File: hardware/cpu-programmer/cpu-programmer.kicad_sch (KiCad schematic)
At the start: 13 parts, among them J1 Conn_01x15_Socket, J2 Conn_01x04_Socket, SW1 SW_Push, SW2 SW_Push

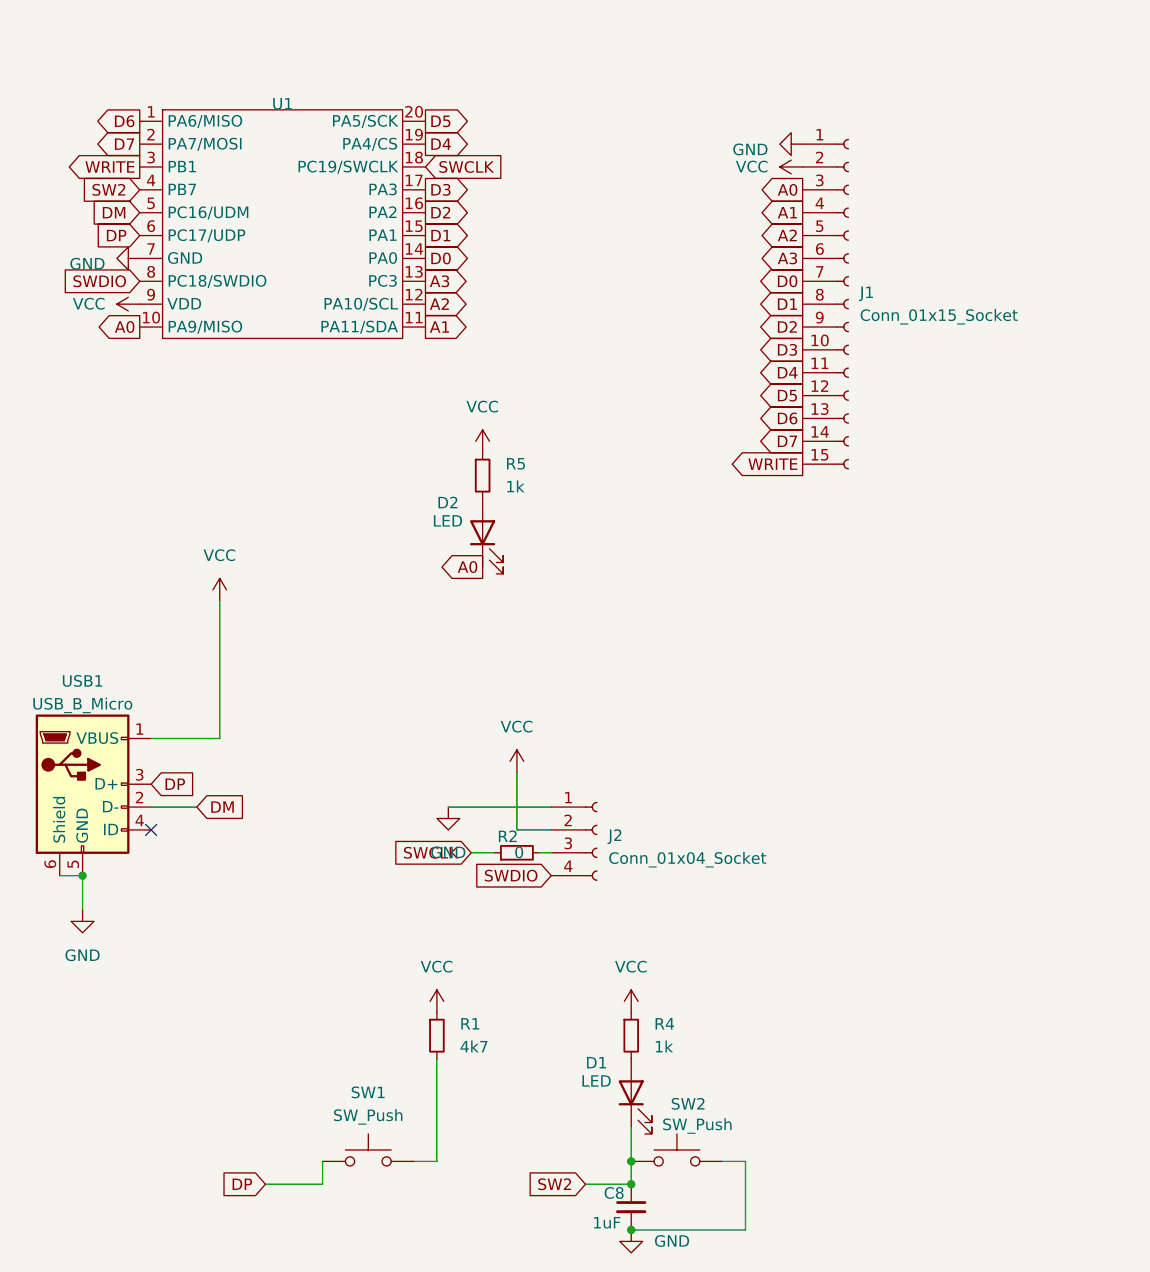
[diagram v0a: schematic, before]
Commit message: Clean up schematic
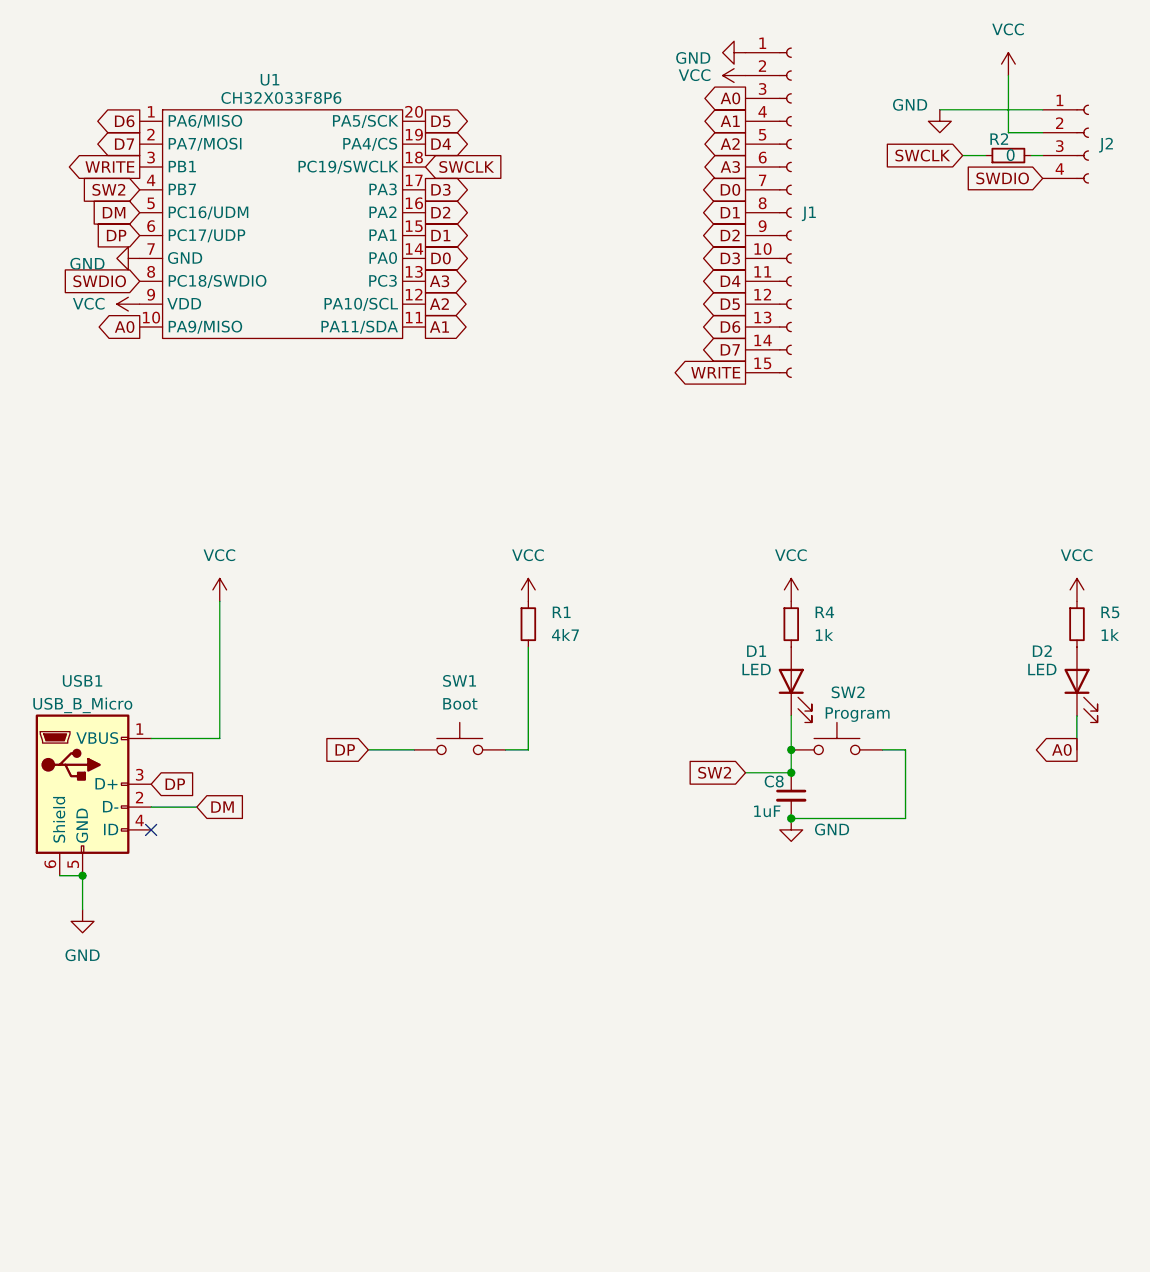
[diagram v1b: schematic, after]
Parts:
- SW1: value SW_Push -> Boot
- SW2: value SW_Push -> Program
- U1: value ~ -> CH32X033F8P6
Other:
- moved on the sheet: C8, D1, D2, J1, J2, R1, R2, R4, R5, SW1, SW2

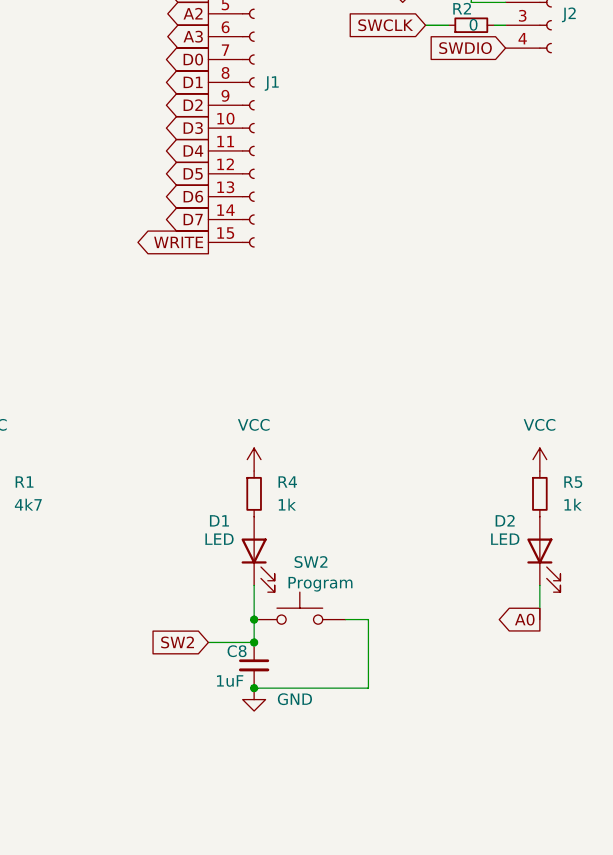
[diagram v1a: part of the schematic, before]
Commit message: Updated PCB, parts use at least package 0603
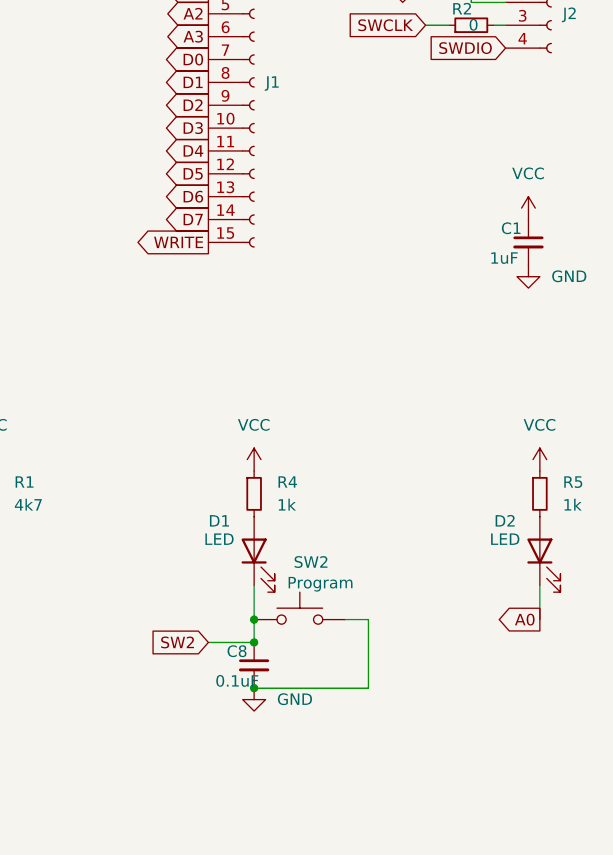
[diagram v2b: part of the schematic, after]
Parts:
- added C1: 1uF, Capacitor_SMD:C_0603_1608Metric, symbol Device:C_Small
- C8: value 1uF -> 0.1uF; footprint Capacitor_SMD:C_0402_1005Metric -> Capacitor_SMD:C_0603_1608Metric
- D1, D2: footprint LED_SMD:LED_0402_1005Metric -> LED_SMD:LED_0603_1608Metric
- R4, R5: footprint Resistor_SMD:R_0402_1005Metric -> Resistor_SMD:R_0603_1608Metric
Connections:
- net GND: now also C1.2
- net VCC: now also C1.1
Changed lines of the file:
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@@
+	(symbol
+		(lib_id "Device:C_Small")
+		(at 137.16 59.69 0)
+		(unit 1)
+		(exclude_from_sim no)
+		(in_bom yes)
+		(on_board yes)
+		(dnp no)
+		(property "Reference" "C1"
+			(at 134.112 58.166 0)
+			(effects
+				(font
+					(size 1.27 1.27)
+				)
+				(justify left)
+			)
+		)
+		(property "Value" "1uF"
+			(at 132.842 61.468 0)
+			(effects
+				(font
+					(size 1.27 1.27)
+				)
+				(justify left)
+			)
+		)
+		(property "Footprint" "Capacitor_SMD:C_0603_1608Metric"
+			(at 137.16 59.69 0)
+			(effects
+				(font
+					(size 1.27 1.27)
+				)
+				(hide yes)
+			)
+		)
+		(property "Datasheet" "~"
+			(at 137.16 59.69 0)
+			(effects
+				(font
+					(size 1.27 1.27)
+				)
+				(hide yes)
+			)
+		)
+		(property "Description" "Unpolarized capacitor, small symbol"
+			(at 137.16 59.69 0)
+			(effects
+				(font
+					(size 1.27 1.27)
+				)
+				(hide yes)
+			)
+		)
+		(pin "1"
+		)
+		(pin "2"
+		)
+		(instances
+			(project "cpu-programmer"
+				(path "/6e692abf-3379-42ed-b901-258ac932806b"
+					(reference "C1")
+					(unit 1)
+				)
+			)
+		)
+	)
+	(symbol
+		(lib_id "power:+3.3V")
+		(at 137.16 57.15 0)
+		(unit 1)
+		(exclude_from_sim no)
+		(in_bom yes)
+		(on_board yes)
+		(dnp no)
+		(fields_autoplaced yes)
+		(property "Reference" "#PWR09"
+			(at 137.16 60.96 0)
+			(effects
+				(font
+					(size 1.27 1.27)
+				)
+				(hide yes)
+			)
+		)
+		(property "Value" "VCC"
+			(at 137.16 52.07 0)
+			(effects
+				(font
+					(size 1.27 1.27)
+				)
+			)
+		)
+		(property "Footprint" ""
+			(at 137.16 57.15 0)
+			(effects
+				(font
+					(size 1.27 1.27)
+				)
+				(hide yes)
+			)
+		)
+		(property "Datasheet" ""
+			(at 137.16 57.15 0)
+			(effects
+				(font
+					(size 1.27 1.27)
+				)
+				(hide yes)
+			)
+		)
+		(property "Description" ""
+			(at 137.16 57.15 0)
+			(effects
+				(font
+					(size 1.27 1.27)
+				)
+			)
+		)
+		(pin "1"
+		)
+		(instances
+			(project "cpu-programmer"
+				(path "/6e692abf-3379-42ed-b901-258ac932806b"
+					(reference "#PWR09")
+					(unit 1)
+				)
+			)
+		)
+	)
+	(symbol
+		(lib_id "power:GND")
+		(at 137.16 62.23 0)
+		(unit 1)
+		(exclude_from_sim no)
+		(in_bom yes)
+		(on_board yes)
+		(dnp no)
+		(fields_autoplaced yes)
+		(property "Reference" "#PWR010"
+			(at 137.16 68.58 0)
+			(effects
+				(font
+					(size 1.27 1.27)
+				)
+				(hide yes)
+			)
+		)
+		(property "Value" "GND"
+			(at 139.7 63.4999 0)
+			(effects
+				(font
+					(size 1.27 1.27)
+				)
+				(justify left)
+			)
+		)
+		(property "Footprint" ""
+			(at 137.16 62.23 0)
+			(effects
+				(font
+					(size 1.27 1.27)
+				)
+				(hide yes)
+			)
+		)
+		(property "Datasheet" ""
+			(at 137.16 62.23 0)
+			(effects
+				(font
+					(size 1.27 1.27)
+				)
+				(hide yes)
+			)
+		)
+		(property "Description" "Power symbol creates a global label with name \"GND\" , ground"
+			(at 137.16 62.23 0)
+			(effects
+				(font
+					(size 1.27 1.27)
+				)
+				(hide yes)
+			)
+		)
+		(pin "1"
+		)
+		(instances
+			(project "cpu-programmer"
+				(path "/6e692abf-3379-42ed-b901-258ac932806b"
+					(reference "#PWR010")
+					(unit 1)
+				)
+			)
+		)
+	)
 	(symbol
 		(lib_id "Device:C_Small")
@@
 			)
 		)
-		(property "Value" "1uF"
+		(property "Value" "0.1uF"
 			(at 102.362 108.458 0)
 			(effects
@@
 			)
 		)
-		(property "Footprint" "Capacitor_SMD:C_0402_1005Metric"
+		(property "Footprint" "Capacitor_SMD:C_0603_1608Metric"
 			(at 106.68 106.68 0)
 			(effects
@@
 			)
 		)
-		(property "Footprint" "LED_SMD:LED_0402_1005Metric"
+		(property "Footprint" "LED_SMD:LED_0603_1608Metric"
 			(at 106.68 93.98 0)
 			(effects
@@
 			)
 		)
-		(property "Footprint" "Resistor_SMD:R_0402_1005Metric"
+		(property "Footprint" "Resistor_SMD:R_0603_1608Metric"
 			(at 138.43 87.63 0)
 			(effects
@@
 			)
 		)
-		(property "Footprint" "Resistor_SMD:R_0402_1005Metric"
+		(property "Footprint" "Resistor_SMD:R_0603_1608Metric"
 			(at 106.68 87.63 0)
 			(effects
@@
 			)
 		)
-		(property "Footprint" "LED_SMD:LED_0402_1005Metric"
+		(property "Footprint" "LED_SMD:LED_0603_1608Metric"
 			(at 138.43 93.98 0)
 			(effects

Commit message: Added gerber
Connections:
- net SWCLK: now also J2.3 (Pin_3), R2.2
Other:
- moved on the sheet: R2
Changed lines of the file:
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@@
+	)
+	(junction
+		(at 129.54 35.56)
+		(diameter 0)
+		(color 0 0 0 0)
 	)
 	(junction
@@
 	)
 	(junction
+		(at 121.92 35.56)
+		(diameter 0)
+		(color 0 0 0 0)
+	)
+	(junction
 		(at 106.68 104.14)
 		(diameter 0)
@@
 	(wire
 		(pts
-			(xy 138.43 101.6) (xy 138.43 97.79)
+			(xy 129.54 34.29) (xy 129.54 35.56)
 		)
 		(stroke
@@
 	(wire
 		(pts
-			(xy 25.4 115.57) (xy 27.94 115.57)
+			(xy 121.92 35.56) (xy 121.92 34.29)
 		)
 		(stroke
@@
 	(wire
 		(pts
-			(xy 77.47 90.17) (xy 77.47 101.6)
+			(xy 138.43 101.6) (xy 138.43 97.79)
 		)
 		(stroke
@@
 	(wire
 		(pts
-			(xy 27.94 115.57) (xy 27.94 119.38)
+			(xy 25.4 115.57) (xy 27.94 115.57)
 		)
 		(stroke
@@
 	(wire
 		(pts
-			(xy 125.73 35.56) (xy 128.27 35.56)
+			(xy 77.47 90.17) (xy 77.47 101.6)
 		)
 		(stroke
@@
 	(wire
 		(pts
-			(xy 134.62 33.02) (xy 130.81 33.02)
+			(xy 27.94 115.57) (xy 27.94 119.38)
 		)
 		(stroke
@@
 	(wire
 		(pts
-			(xy 130.81 33.02) (xy 130.81 26.67)
+			(xy 129.54 35.56) (xy 134.62 35.56)
 		)
 		(stroke
@@
 	(wire
 		(pts
-			(xy 74.93 101.6) (xy 77.47 101.6)
+			(xy 120.65 35.56) (xy 121.92 35.56)
 		)
 		(stroke
@@
 	(wire
 		(pts
-			(xy 133.35 35.56) (xy 134.62 35.56)
+			(xy 134.62 33.02) (xy 130.81 33.02)
 		)
 		(stroke
@@
 	(wire
 		(pts
-			(xy 106.68 109.22) (xy 119.38 109.22)
+			(xy 130.81 33.02) (xy 130.81 26.67)
 		)
 		(stroke
@@
 	(wire
 		(pts
-			(xy 35.56 100.33) (xy 43.18 100.33)
+			(xy 74.93 101.6) (xy 77.47 101.6)
 		)
 		(stroke
@@
 	(wire
 		(pts
-			(xy 119.38 101.6) (xy 119.38 109.22)
+			(xy 128.27 35.56) (xy 129.54 35.56)
 		)
 		(stroke
@@
 	(wire
 		(pts
-			(xy 123.19 30.48) (xy 134.62 30.48)
+			(xy 106.68 109.22) (xy 119.38 109.22)
 		)
 		(stroke
@@
 	(wire
 		(pts
-			(xy 106.68 101.6) (xy 106.68 104.14)
+			(xy 35.56 100.33) (xy 43.18 100.33)
 		)
 		(stroke
@@
 	(wire
 		(pts
-			(xy 106.68 101.6) (xy 106.68 97.79)
+			(xy 119.38 101.6) (xy 119.38 109.22)
 		)
 		(stroke
@@
 	(wire
 		(pts
-			(xy 59.69 101.6) (xy 64.77 101.6)
+			(xy 115.57 30.48) (xy 134.62 30.48)
 		)
 		(stroke
@@
 	(wire
 		(pts
-			(xy 43.18 85.09) (xy 43.18 100.33)
+			(xy 121.92 35.56) (xy 123.19 35.56)
 		)
 		(stroke
@@
 	(wire
 		(pts
-			(xy 116.84 101.6) (xy 119.38 101.6)
+			(xy 106.68 101.6) (xy 106.68 104.14)
 		)
 		(stroke
@@
 		)
 	)
+	(wire
+		(pts
+			(xy 106.68 101.6) (xy 106.68 97.79)
+		)
+		(stroke
+			(width 0)
+			(type default)
+		)
+	)
+	(wire
+		(pts
+			(xy 121.92 34.29) (xy 129.54 34.29)
+		)
+		(stroke
+			(width 0)
+			(type default)
+		)
+	)
+	(wire
+		(pts
+			(xy 59.69 101.6) (xy 64.77 101.6)
+		)
+		(stroke
+			(width 0)
+			(type default)
+		)
+	)
+	(wire
+		(pts
+			(xy 43.18 85.09) (xy 43.18 100.33)
+		)
+		(stroke
+			(width 0)
+			(type default)
+		)
+	)
+	(wire
+		(pts
+			(xy 116.84 101.6) (xy 119.38 101.6)
+		)
+		(stroke
+			(width 0)
+			(type default)
+		)
+	)
 	(global_label "D0"
 		(shape output)
@@
 	(global_label "SWCLK"
 		(shape input)
-		(at 125.73 35.56 180)
+		(at 120.65 35.56 180)
 		(fields_autoplaced yes)
 		(effects
@@
 		)
 		(property "Intersheetrefs" "${INTERSHEET_REFS}"
-			(at 116.5952 35.56 0)
+			(at 111.5152 35.56 0)
 			(effects
 				(font
@@
 	(symbol
 		(lib_id "power:GND")
-		(at 123.19 30.48 0)
+		(at 115.57 30.48 0)
 		(unit 1)
 		(exclude_from_sim no)
@@
 		(dnp no)
 		(property "Reference" "#PWR017"
-			(at 123.19 36.83 0)
+			(at 115.57 36.83 0)
 			(effects
 				(font
@@
 		)
 		(property "Value" "GND"
-			(at 119.888 29.972 0)
+			(at 112.268 29.972 0)
 			(effects
 				(font
@@
 		)
 		(property "Footprint" ""
-			(at 123.19 30.48 0)
+			(at 115.57 30.48 0)
 			(effects
 				(font
@@
 		)
 		(property "Datasheet" ""
-			(at 123.19 30.48 0)
+			(at 115.57 30.48 0)
 			(effects
 				(font
@@
 		)
 		(property "Description" ""
-			(at 123.19 30.48 0)
+			(at 115.57 30.48 0)
 			(effects
 				(font
@@
 	(symbol
 		(lib_id "Device:R_Small")
-		(at 130.81 35.56 90)
+		(at 125.73 35.56 90)
 		(unit 1)
 		(exclude_from_sim no)
@@
 		(dnp no)
 		(property "Reference" "R2"
-			(at 129.794 33.782 90)
+			(at 124.714 33.782 90)
 			(effects
 				(font
@@
 		)
 		(property "Value" "0"
-			(at 131.064 35.56 90)
+			(at 125.984 35.56 90)
 			(effects
 				(font
@@
 		)
 		(property "Footprint" "Resistor_SMD:R_1206_3216Metric"
-			(at 130.81 35.56 0)
+			(at 125.73 35.56 0)
 			(effects
 				(font
@@
 		)
 		(property "Datasheet" "~"
-			(at 130.81 35.56 0)
+			(at 125.73 35.56 0)
 			(effects
 				(font
@@
 		)
 		(property "Description" "Resistor, small symbol"
-			(at 130.81 35.56 0)
-			(effects
-				(font
+			(at 125.73 35.56 0)
+			(effects
+				(font

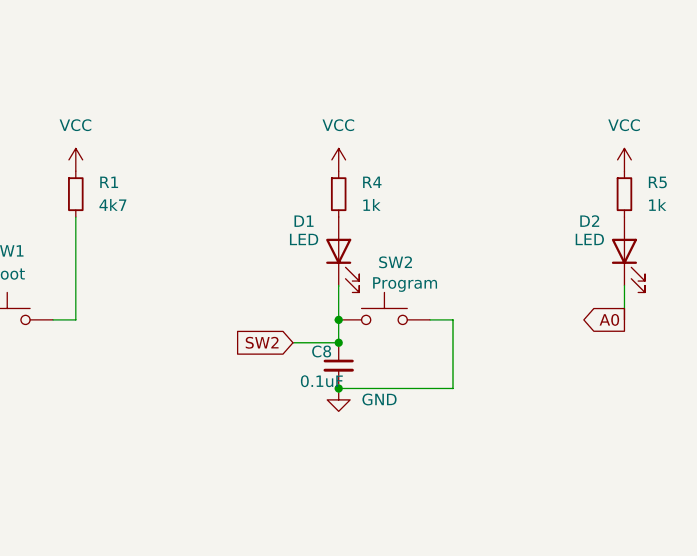
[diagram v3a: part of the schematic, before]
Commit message: Updated PCB
Fixed silkscreen lables
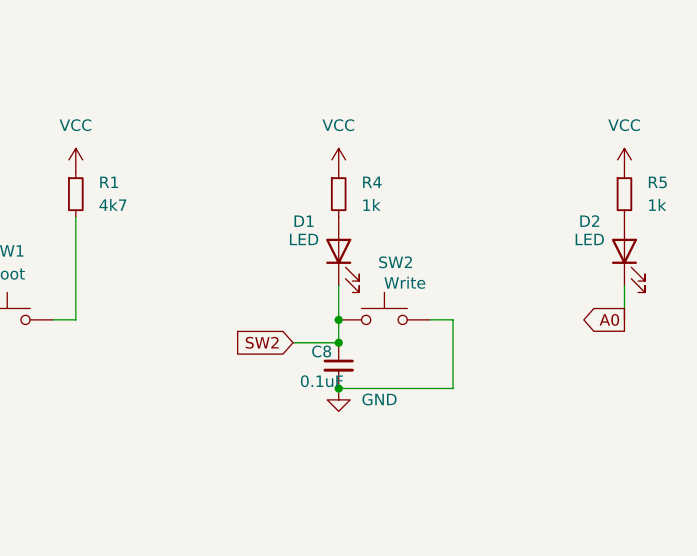
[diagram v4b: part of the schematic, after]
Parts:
- SW2: value Program -> Write
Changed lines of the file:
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@@
 			)
 		)
-		(property "Value" "Program"
+		(property "Value" "Write"
 			(at 114.046 97.536 0)
 			(effects
